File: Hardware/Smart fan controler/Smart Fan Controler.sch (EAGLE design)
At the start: 37 parts

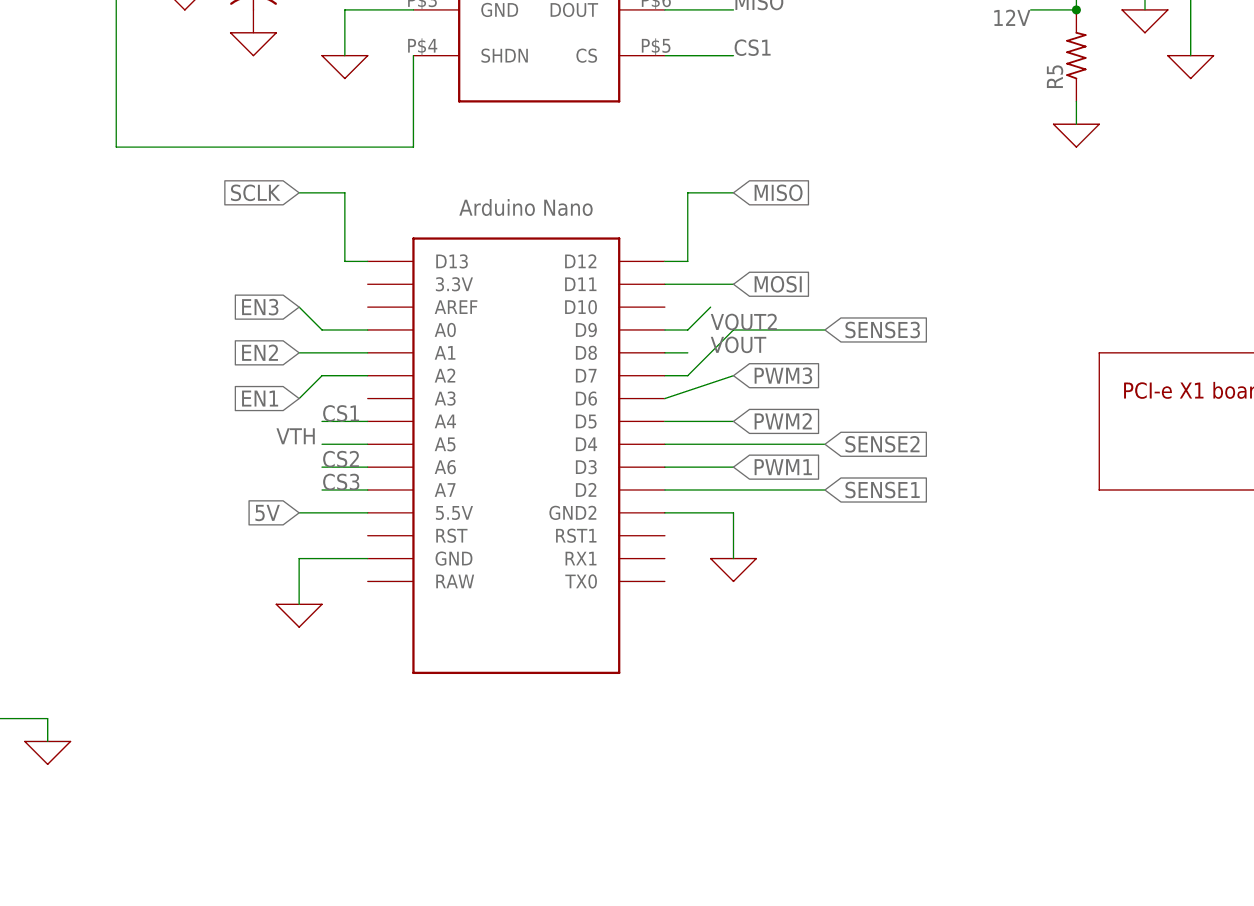
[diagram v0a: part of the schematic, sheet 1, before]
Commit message: Added legend to clarify pin connections
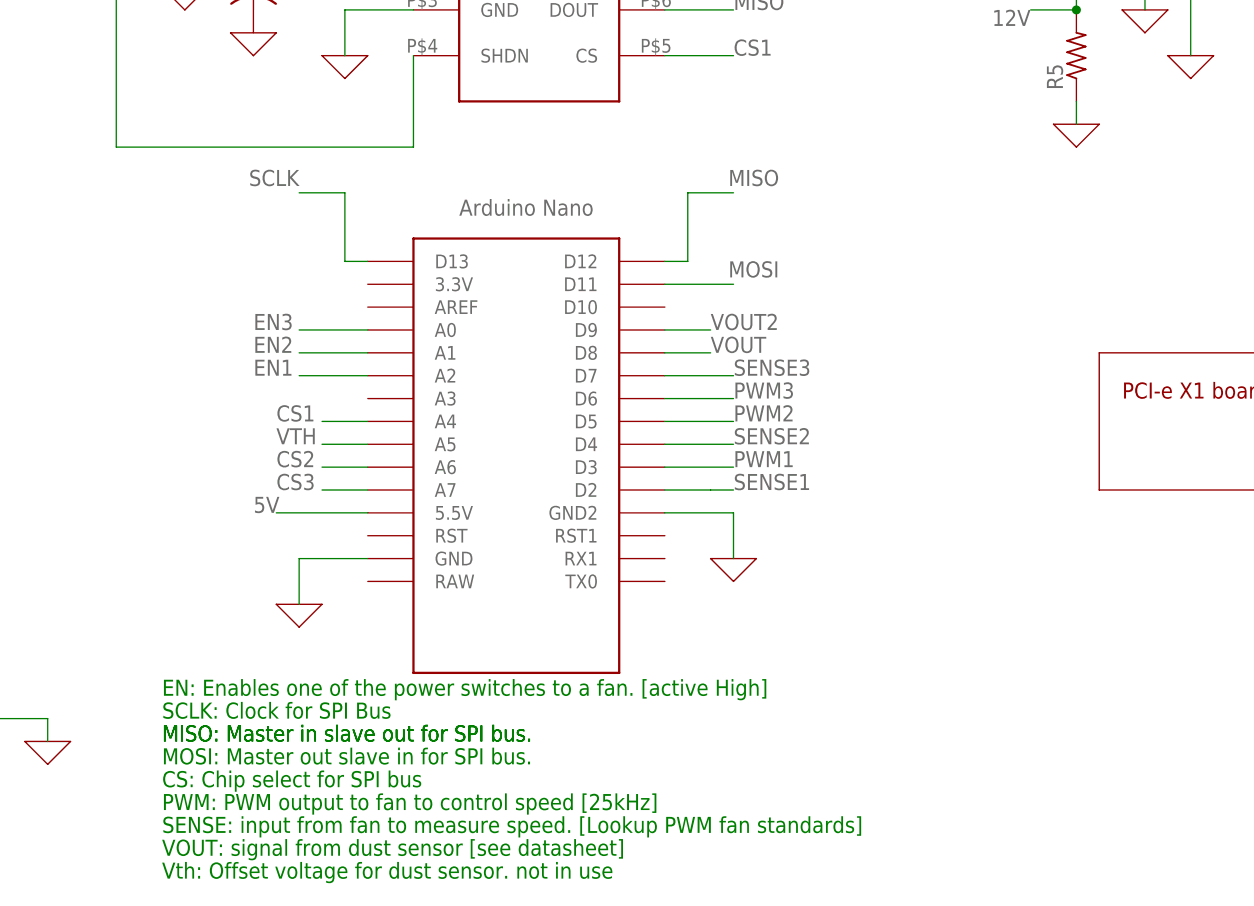
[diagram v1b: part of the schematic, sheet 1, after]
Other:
- note added: "CS: Chip select for SPI bus"
- note added: "EN: Enables one of the power switches to a fan. [active High]"
- note added: "MISO: Master in slave out for SPI bus."
- note added: "MOSI: Master out slave in for SPI bus."
- note added: "PWM: PWM output to fan to control speed [25kHz]"
- note added: "SCLK: Clock for SPI Bus"
- note added: "SENSE: input from fan to measure speed. [Lookup PWM fan standards]"
- note added: "VOUT: signal from dust sensor [see datasheet]"
- note added: "Vth: Offset voltage for dust sensor. not in use"
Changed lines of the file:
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@@
 <wire x1="142.24" y1="53.34" x2="111.76" y2="53.34" width="0.1524" layer="94"/>
 <wire x1="111.76" y1="53.34" x2="111.76" y2="38.1" width="0.1524" layer="94"/>
+<text x="7.62" y="15.24" size="1.778" layer="91">EN: Enables one of the power switches to a fan. [active High] </text>
+<text x="7.62" y="12.7" size="1.778" layer="91">SCLK: Clock for SPI Bus</text>
+<text x="7.62" y="10.16" size="1.778" layer="91">MISO: Master in slave out for SPI bus.</text>
+<text x="7.62" y="10.16" size="1.778" layer="91">MISO: Master in slave out for SPI bus.</text>
+<text x="7.62" y="7.62" size="1.778" layer="91">MOSI: Master out slave in for SPI bus.</text>
+<text x="7.62" y="5.08" size="1.778" layer="91">CS: Chip select for SPI bus</text>
+<text x="7.62" y="2.54" size="1.778" layer="91">PWM: PWM output to fan to control speed [25kHz]</text>
+<text x="7.62" y="0" size="1.778" layer="91">SENSE: input from fan to measure speed. [Lookup PWM fan standards]</text>
+<text x="7.62" y="-2.54" size="1.778" layer="91">VOUT: signal from dust sensor [see datasheet]</text>
+<text x="7.62" y="-5.08" size="1.778" layer="91">Vth: Offset voltage for dust sensor. not in use </text>
 </plain>
 <instances>
@@
 <wire x1="27.94" y1="63.5" x2="27.94" y2="71.12" width="0.1524" layer="91"/>
 <wire x1="27.94" y1="71.12" x2="22.86" y2="71.12" width="0.1524" layer="91"/>
-<label x="22.86" y="71.12" size="1.778" layer="95" rot="R180" xref="yes"/>
+<label x="22.86" y="73.66" size="1.778" layer="95" rot="R180"/>
 </segment>
 <segment>
@@
 <pinref part="U$2" gate="G$1" pin="A4"/>
 <wire x1="30.48" y1="45.72" x2="25.4" y2="45.72" width="0.1524" layer="91"/>
-<label x="25.4" y="45.72" size="1.778" layer="95"/>
+<label x="20.32" y="45.72" size="1.778" layer="95"/>
 </segment>
 </net>
@@
 <wire x1="66.04" y1="63.5" x2="66.04" y2="71.12" width="0.1524" layer="91"/>
 <wire x1="66.04" y1="71.12" x2="71.12" y2="71.12" width="0.1524" layer="91"/>
-<label x="71.12" y="71.12" size="1.778" layer="95" xref="yes"/>
+<label x="76.2" y="73.66" size="1.778" layer="95" rot="R180"/>
 </segment>
 <segment>
@@
 <pinref part="U$2" gate="G$1" pin="D11"/>
 <wire x1="63.5" y1="60.96" x2="71.12" y2="60.96" width="0.1524" layer="91"/>
-<label x="71.12" y="60.96" size="1.778" layer="95" xref="yes"/>
+<label x="76.2" y="63.5" size="1.778" layer="95" rot="R180"/>
 </segment>
 <segment>
@@
 <segment>
 <pinref part="U$2" gate="G$1" pin="5.5V"/>
-<wire x1="30.48" y1="35.56" x2="22.86" y2="35.56" width="0.1524" layer="91"/>
-<label x="22.86" y="35.56" size="1.778" layer="95" rot="R180" xref="yes"/>
+<label x="17.78" y="35.56" size="1.778" layer="95"/>
+<wire x1="30.48" y1="35.56" x2="20.32" y2="35.56" width="0.1524" layer="91"/>
 </segment>
 <segment>
@@
 <pinref part="U$2" gate="G$1" pin="A6"/>
 <wire x1="30.48" y1="40.64" x2="25.4" y2="40.64" width="0.1524" layer="91"/>
-<label x="25.4" y="40.64" size="1.778" layer="95"/>
+<label x="20.32" y="40.64" size="1.778" layer="95"/>
 </segment>
 </net>
@@
 <pinref part="U$2" gate="G$1" pin="A7"/>
 <wire x1="30.48" y1="38.1" x2="25.4" y2="38.1" width="0.1524" layer="91"/>
-<label x="25.4" y="38.1" size="1.778" layer="95"/>
+<label x="20.32" y="38.1" size="1.778" layer="95"/>
 </segment>
 </net>
@@
 <segment>
 <pinref part="U$2" gate="G$1" pin="A0"/>
-<wire x1="30.48" y1="55.88" x2="25.4" y2="55.88" width="0.1524" layer="91"/>
-<wire x1="25.4" y1="55.88" x2="22.86" y2="58.42" width="0.1524" layer="91"/>
-<label x="22.86" y="58.42" size="1.778" layer="95" rot="R180" xref="yes"/>
+<wire x1="30.48" y1="55.88" x2="22.86" y2="55.88" width="0.1524" layer="91"/>
+<label x="17.78" y="55.88" size="1.778" layer="95"/>
 </segment>
 </net>
@@
 <segment>
 <pinref part="U$2" gate="G$1" pin="A2"/>
-<wire x1="30.48" y1="50.8" x2="25.4" y2="50.8" width="0.1524" layer="91"/>
-<wire x1="25.4" y1="50.8" x2="22.86" y2="48.26" width="0.1524" layer="91"/>
-<label x="22.86" y="48.26" size="1.778" layer="95" rot="R180" xref="yes"/>
+<wire x1="30.48" y1="50.8" x2="22.86" y2="50.8" width="0.1524" layer="91"/>
+<label x="17.78" y="50.8" size="1.778" layer="95"/>
 </segment>
 <segment>
@@
 <pinref part="U$2" gate="G$1" pin="A1"/>
 <wire x1="30.48" y1="53.34" x2="22.86" y2="53.34" width="0.1524" layer="91"/>
-<label x="22.86" y="53.34" size="1.778" layer="95" rot="R180" xref="yes"/>
+<label x="17.78" y="53.34" size="1.778" layer="95"/>
 </segment>
 <segment>
@@
 <pinref part="U$2" gate="G$1" pin="D3"/>
 <wire x1="63.5" y1="40.64" x2="71.12" y2="40.64" width="0.1524" layer="91"/>
-<label x="71.12" y="40.64" size="1.778" layer="95" xref="yes"/>
+<label x="71.12" y="40.64" size="1.778" layer="95"/>
 </segment>
 <segment>
@@
 <pinref part="U$2" gate="G$1" pin="D5"/>
 <wire x1="63.5" y1="45.72" x2="71.12" y2="45.72" width="0.1524" layer="91"/>
-<label x="71.12" y="45.72" size="1.778" layer="95" xref="yes"/>
+<label x="71.12" y="45.72" size="1.778" layer="95"/>
 </segment>
 <segment>
@@
 <segment>
 <pinref part="U$2" gate="G$1" pin="D6"/>
-<wire x1="63.5" y1="48.26" x2="71.12" y2="50.8" width="0.1524" layer="91"/>
-<label x="71.12" y="50.8" size="1.778" layer="95" xref="yes"/>
+<wire x1="63.5" y1="48.26" x2="71.12" y2="48.26" width="0.1524" layer="91"/>
+<label x="71.12" y="48.26" size="1.778" layer="95"/>
 </segment>
 </net>
@@
 <segment>
 <pinref part="U$2" gate="G$1" pin="D2"/>
-<wire x1="63.5" y1="38.1" x2="81.28" y2="38.1" width="0.1524" layer="91"/>
-<label x="81.28" y="38.1" size="1.778" layer="95" xref="yes"/>
+<wire x1="63.5" y1="38.1" x2="68.58" y2="38.1" width="0.1524" layer="91"/>
+<label x="71.12" y="38.1" size="1.778" layer="95"/>
+<wire x1="71.12" y1="38.1" x2="68.58" y2="38.1" width="0.1524" layer="91"/>
 </segment>
 <segment>
@@
 <segment>
 <pinref part="U$2" gate="G$1" pin="D4"/>
-<wire x1="63.5" y1="43.18" x2="81.28" y2="43.18" width="0.1524" layer="91"/>
-<label x="81.28" y="43.18" size="1.778" layer="95" xref="yes"/>
+<wire x1="63.5" y1="43.18" x2="71.12" y2="43.18" width="0.1524" layer="91"/>
+<label x="71.12" y="43.18" size="1.778" layer="95"/>
 </segment>
 <segment>
@@
 <segment>
 <pinref part="U$2" gate="G$1" pin="D7"/>
-<wire x1="63.5" y1="50.8" x2="66.04" y2="50.8" width="0.1524" layer="91"/>
-<wire x1="66.04" y1="50.8" x2="71.12" y2="55.88" width="0.1524" layer="91"/>
-<wire x1="71.12" y1="55.88" x2="81.28" y2="55.88" width="0.1524" layer="91"/>
-<label x="81.28" y="55.88" size="1.778" layer="95" xref="yes"/>
+<wire x1="63.5" y1="50.8" x2="71.12" y2="50.8" width="0.1524" layer="91"/>
+<label x="71.12" y="50.8" size="1.778" layer="95"/>
 </segment>
 <segment>
@@
 <segment>
 <pinref part="U$2" gate="G$1" pin="D9"/>
-<wire x1="63.5" y1="55.88" x2="66.04" y2="55.88" width="0.1524" layer="91"/>
-<wire x1="66.04" y1="55.88" x2="68.58" y2="58.42" width="0.1524" layer="91"/>
+<wire x1="63.5" y1="55.88" x2="68.58" y2="55.88" width="0.1524" layer="91"/>
 <label x="68.58" y="55.88" size="1.778" layer="95"/>
 </segment>
@@
 <segment>
 <pinref part="U$2" gate="G$1" pin="D8"/>
-<wire x1="63.5" y1="53.34" x2="66.04" y2="53.34" width="0.1524" layer="91"/>
+<wire x1="63.5" y1="53.34" x2="68.58" y2="53.34" width="0.1524" layer="91"/>
 <label x="68.58" y="53.34" size="1.778" layer="95"/>
 </segment>
